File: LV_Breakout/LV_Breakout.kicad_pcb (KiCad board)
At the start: 2 copper layers, 101.6 x 90.8 mm, 43 parts, among them J1 B10B-PHDSS(LF)(SN), J2 DF22-2P-7.92DSA(05), J3 TE 1-770872-0, J4 TE 776228-1, K1 T9VV1K15-12S, Q1 CSD18563Q5A, U1 R-78E5.0-0.5, U2 LM74700QDBVTQ1, U3 INA219AIDR, U4 INA219AIDR

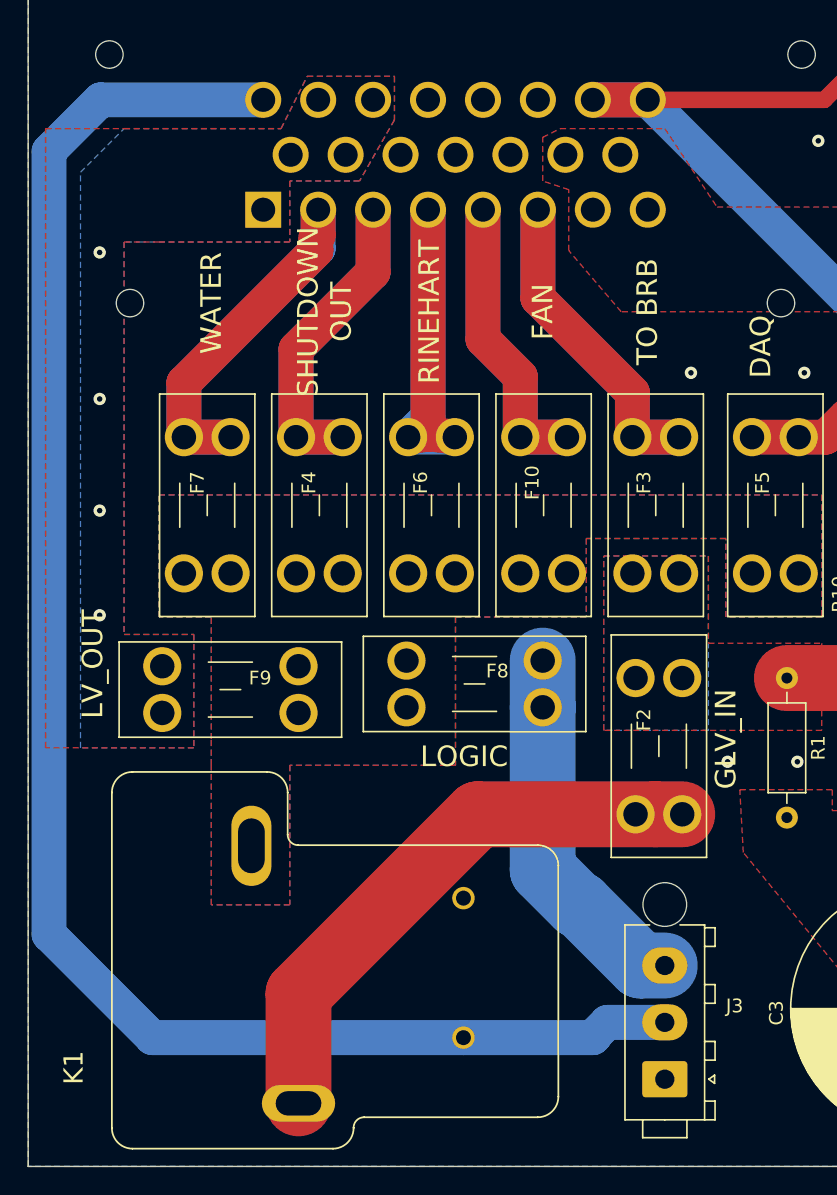
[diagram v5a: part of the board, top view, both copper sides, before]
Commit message: change pcb trace
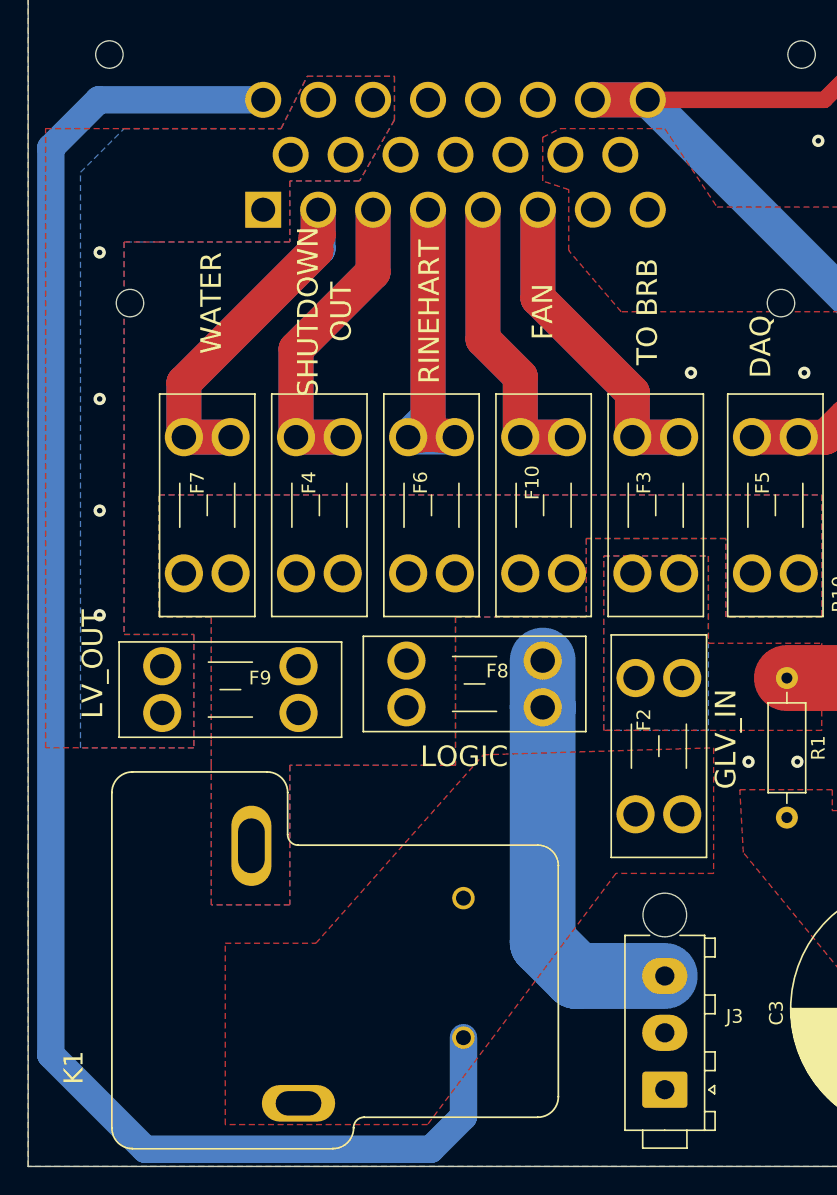
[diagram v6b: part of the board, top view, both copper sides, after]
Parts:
- removed G***: LOGO, AERO_CUSTOM:AERO_Logo_15x6mm
- moved J3 0.76 mm to (154.9, 108.7)
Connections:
- net Net-(F2-Pad2) renamed /Main_GLV
- J3 pad 2: /FROM_BRB -> (no net)
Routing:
- net /Main_GLV: track 41.3 -> 0.00 mm
- net /LOGIC: track 27.0 -> 30.4 mm
- added copper zone on F.Cu, net /Main_GLV

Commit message: Minor Layout Changes
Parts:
- J2: footprint Connector_JST:JST_VH_B2P3-VH_1x02_P7.92mm_Vertical -> AERO_FOOT:DF22-2P-7.92DSA05
- turned J2 to 90 degrees

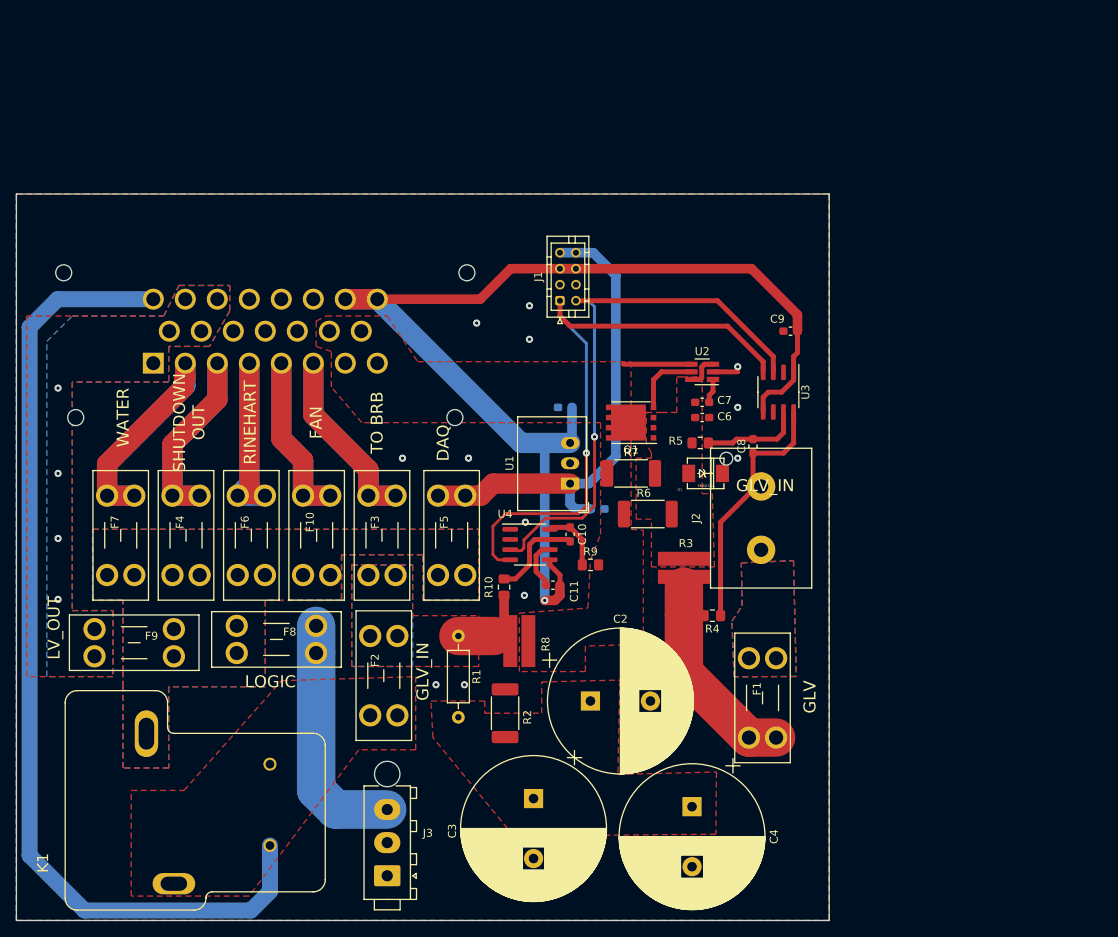
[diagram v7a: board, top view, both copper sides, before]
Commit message: Change trace and create Gerber
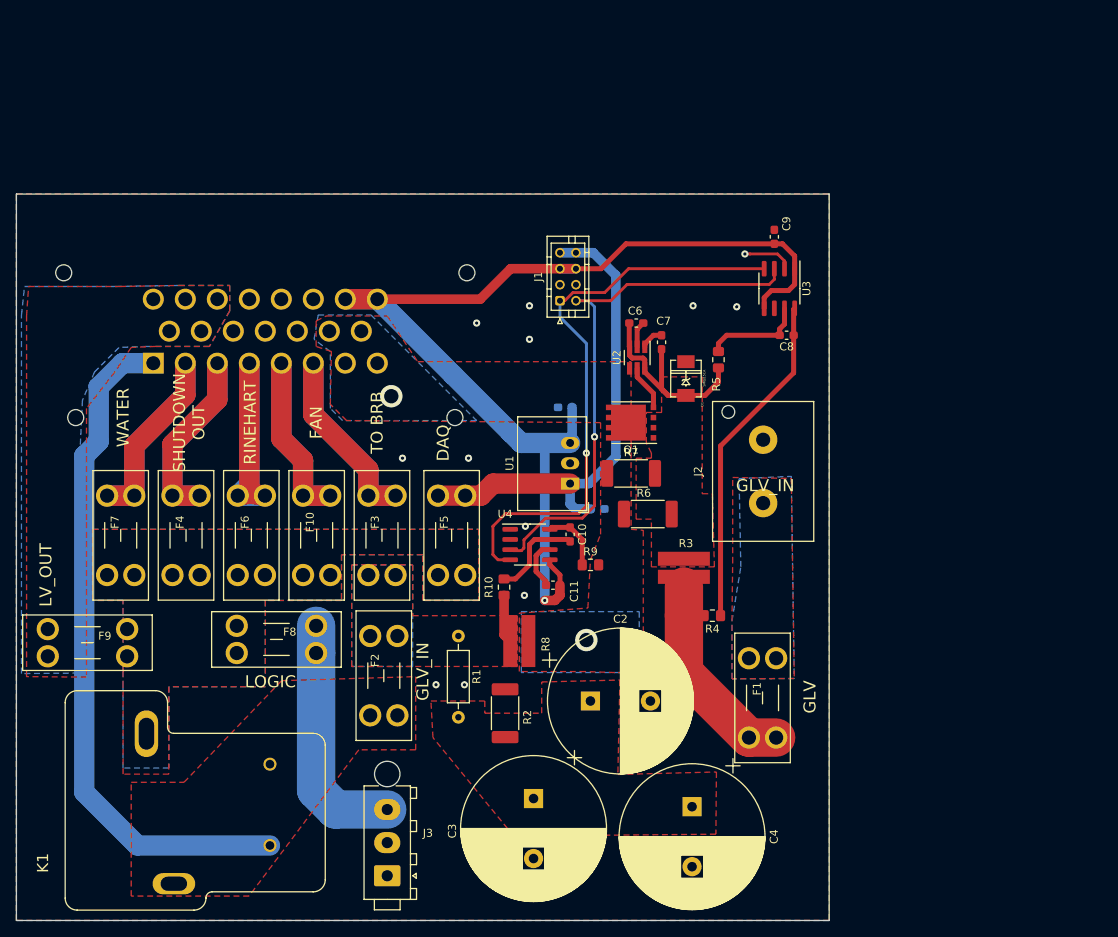
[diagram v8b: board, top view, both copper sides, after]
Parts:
- moved C8 14.5 mm to (204.9, 41.1), turned to 180 degrees
- moved C6 14.4 mm to (186.1, 39.6)
- moved U3 13.0 mm to (204.0, 35.3)
- moved D1 12.1 mm to (192.3, 46.6), turned to 90 degrees
- moved C9 12.0 mm to (203.3, 28.8), turned to 90 degrees
- moved R5 10.7 mm to (196.3, 44.2), turned to 270 degrees
- moved C7 9.06 mm to (189.2, 42.0), turned to 270 degrees
- moved U2 8.32 mm to (186.2, 43.9), turned to 270 degrees
- moved J2 5.85 mm to (201.9, 58.2)
- moved F9 5.84 mm to (122.4, 81.3)
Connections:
- J4 pad 1: /LV_PWR -> /FROM_BRB
- J4 pad 16: /FROM_BRB -> /LV_PWR
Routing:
- net /FROM_BRB: track 122.6 -> 85.4 mm
- net /GLV_COMB/VBATT_CUROUT: track 4.28 -> 26.7 mm
- net Net-(C8-Pad1): track 31.5 -> 42.3 mm
- net /DCDC_IN: track 8.50 -> 0.00 mm, vias 0 -> 2
- net GND: track 9.33 -> 15.8 mm
- net +5V: track 147.0 -> 140.7 mm
- net /GLV_IN: track 10.5 -> 6.04 mm
- net /SCL: track 76.7 -> 72.9 mm
- net Net-(Q1-Pad2): track 8.59 -> 5.72 mm
- net /COOL_PWR: track 48.0 -> 45.2 mm
- net /SDA: track 70.6 -> 68.3 mm
- net /LV_PWR: vias 4 -> 0
- added copper zone on B.Cu, net /DCDC_IN
